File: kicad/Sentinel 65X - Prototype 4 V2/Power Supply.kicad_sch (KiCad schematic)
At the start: 32 parts, among them J7 GCT_USB4085, J8 Power Switch, U10 TPS63001, U11 TPS63002, U12 FT230XS

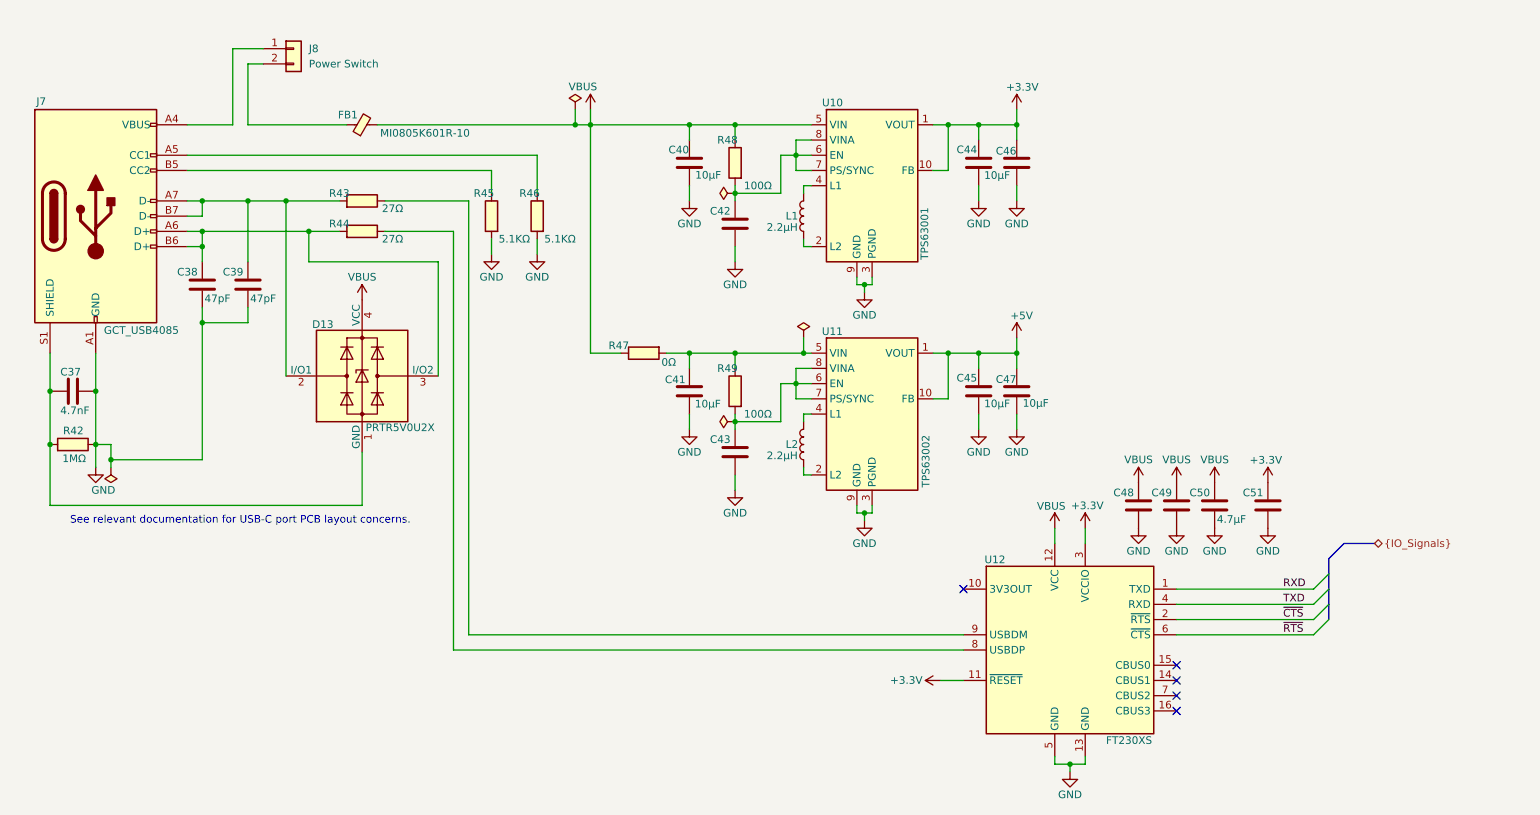
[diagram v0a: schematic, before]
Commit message: Updated prototype 4V2 schematic
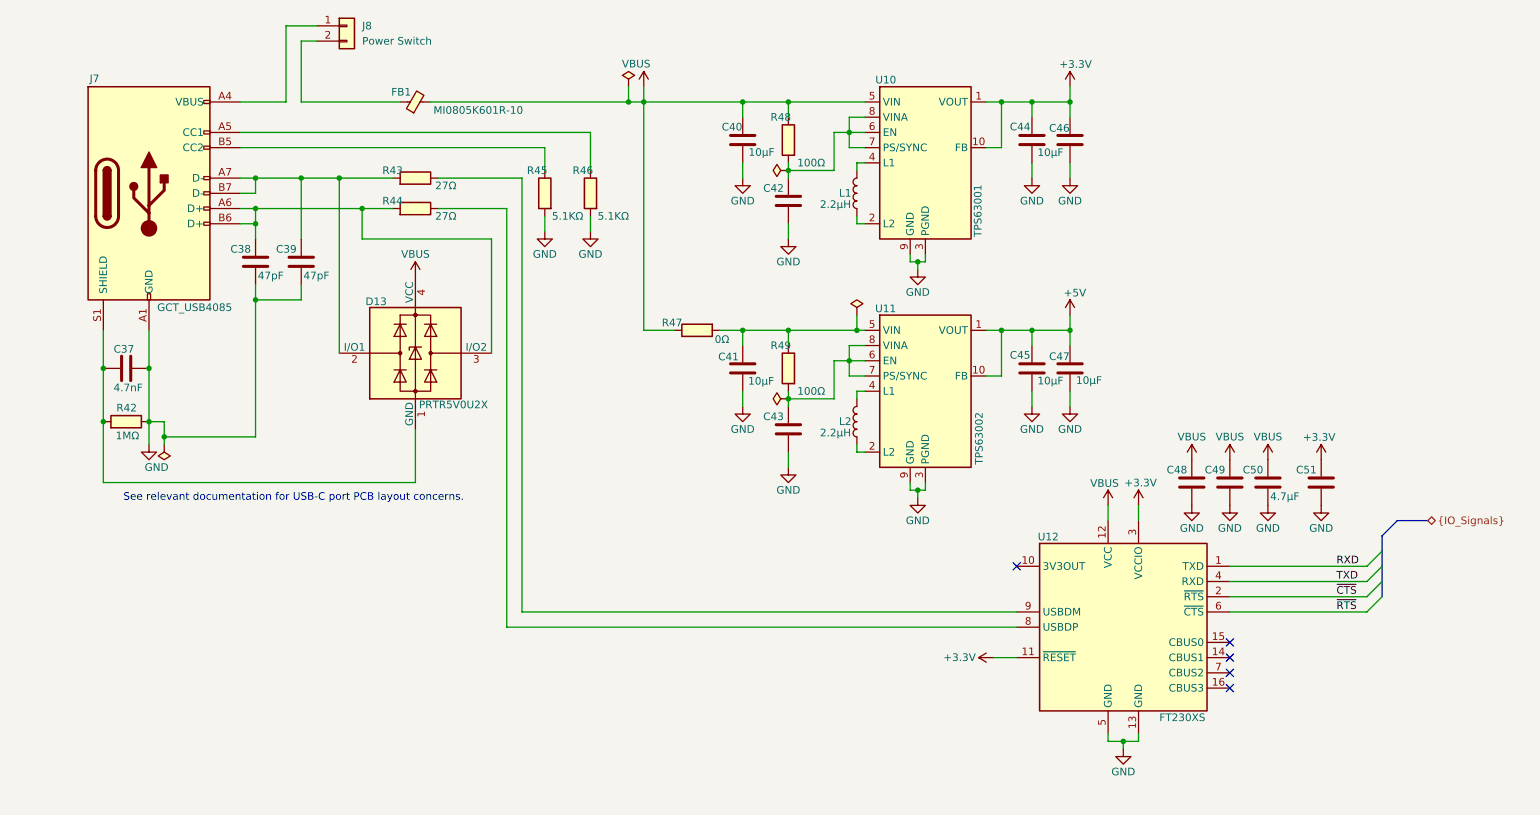
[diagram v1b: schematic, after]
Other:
- moved on the sheet: C37, C38, C39, C40, C41, C42, C43, C44, C45, C46, C47, C48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
